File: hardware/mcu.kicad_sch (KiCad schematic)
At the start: 27 parts, among them J4 PROG, U6 RP2040, U9 IS25LP080D-JBLE, Y1 2TJ412000NYGBC

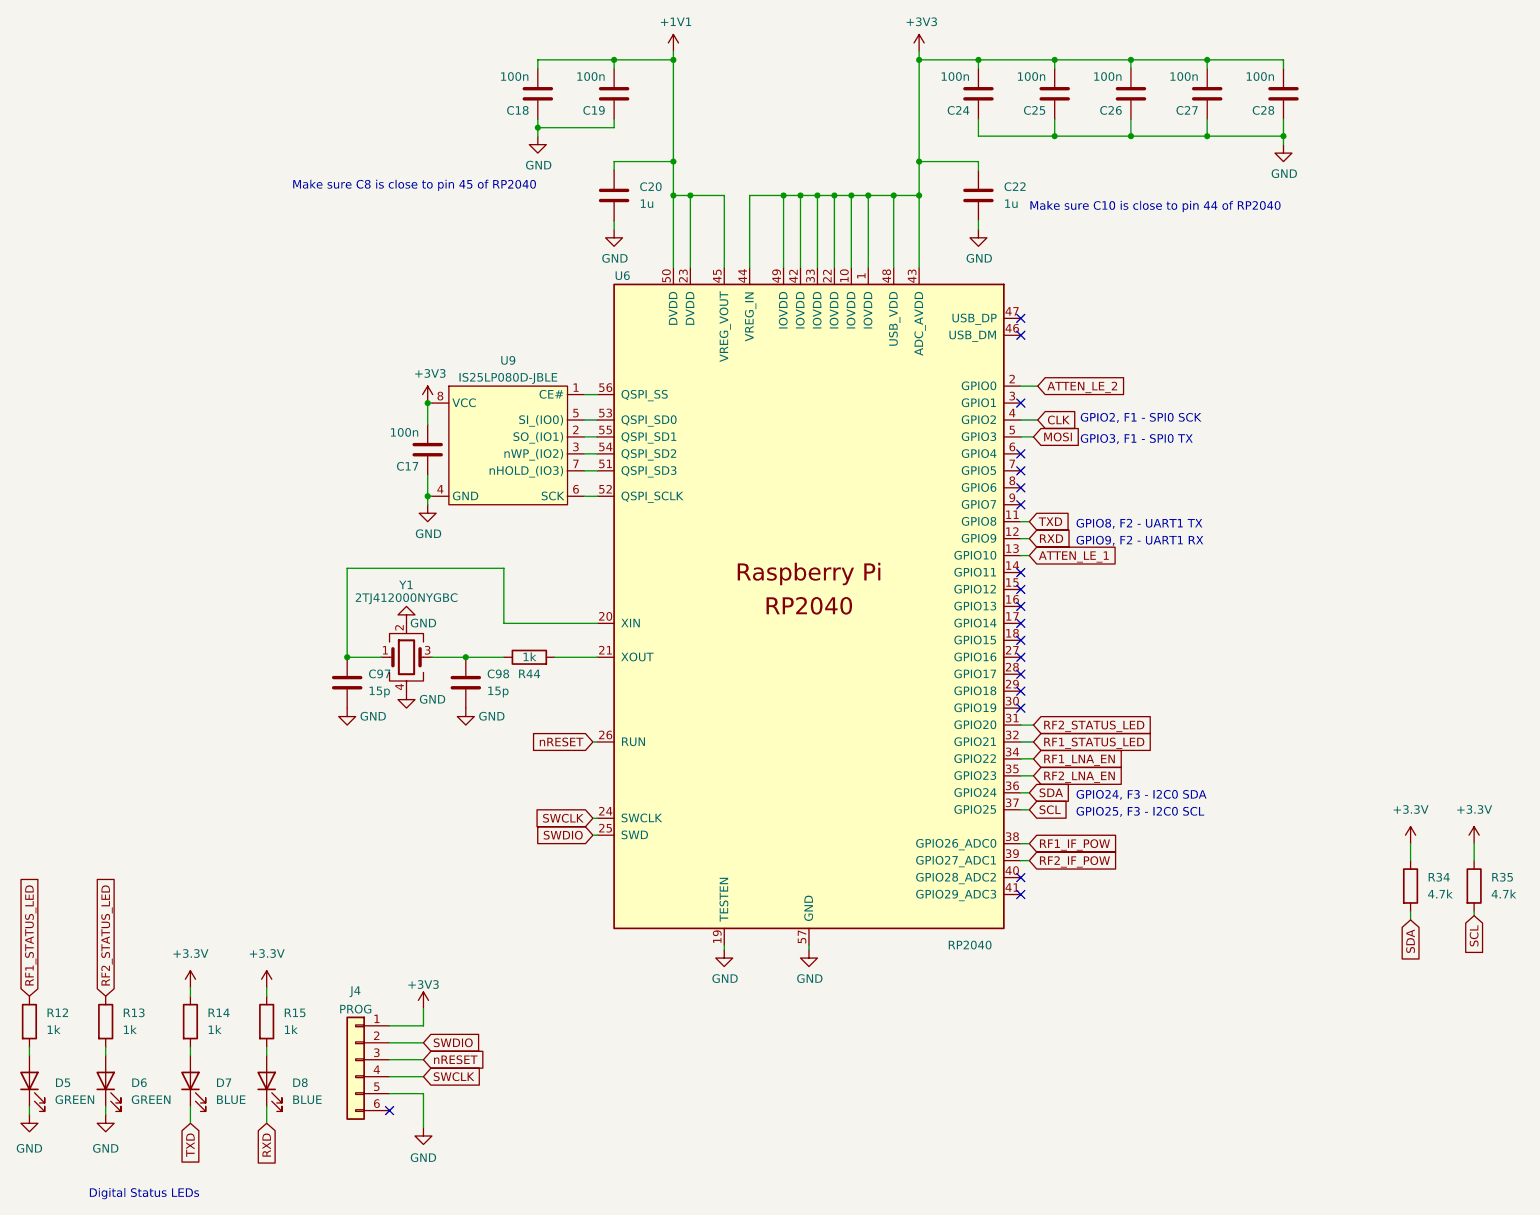
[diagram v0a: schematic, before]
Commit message: Update FEM hardware design for production version
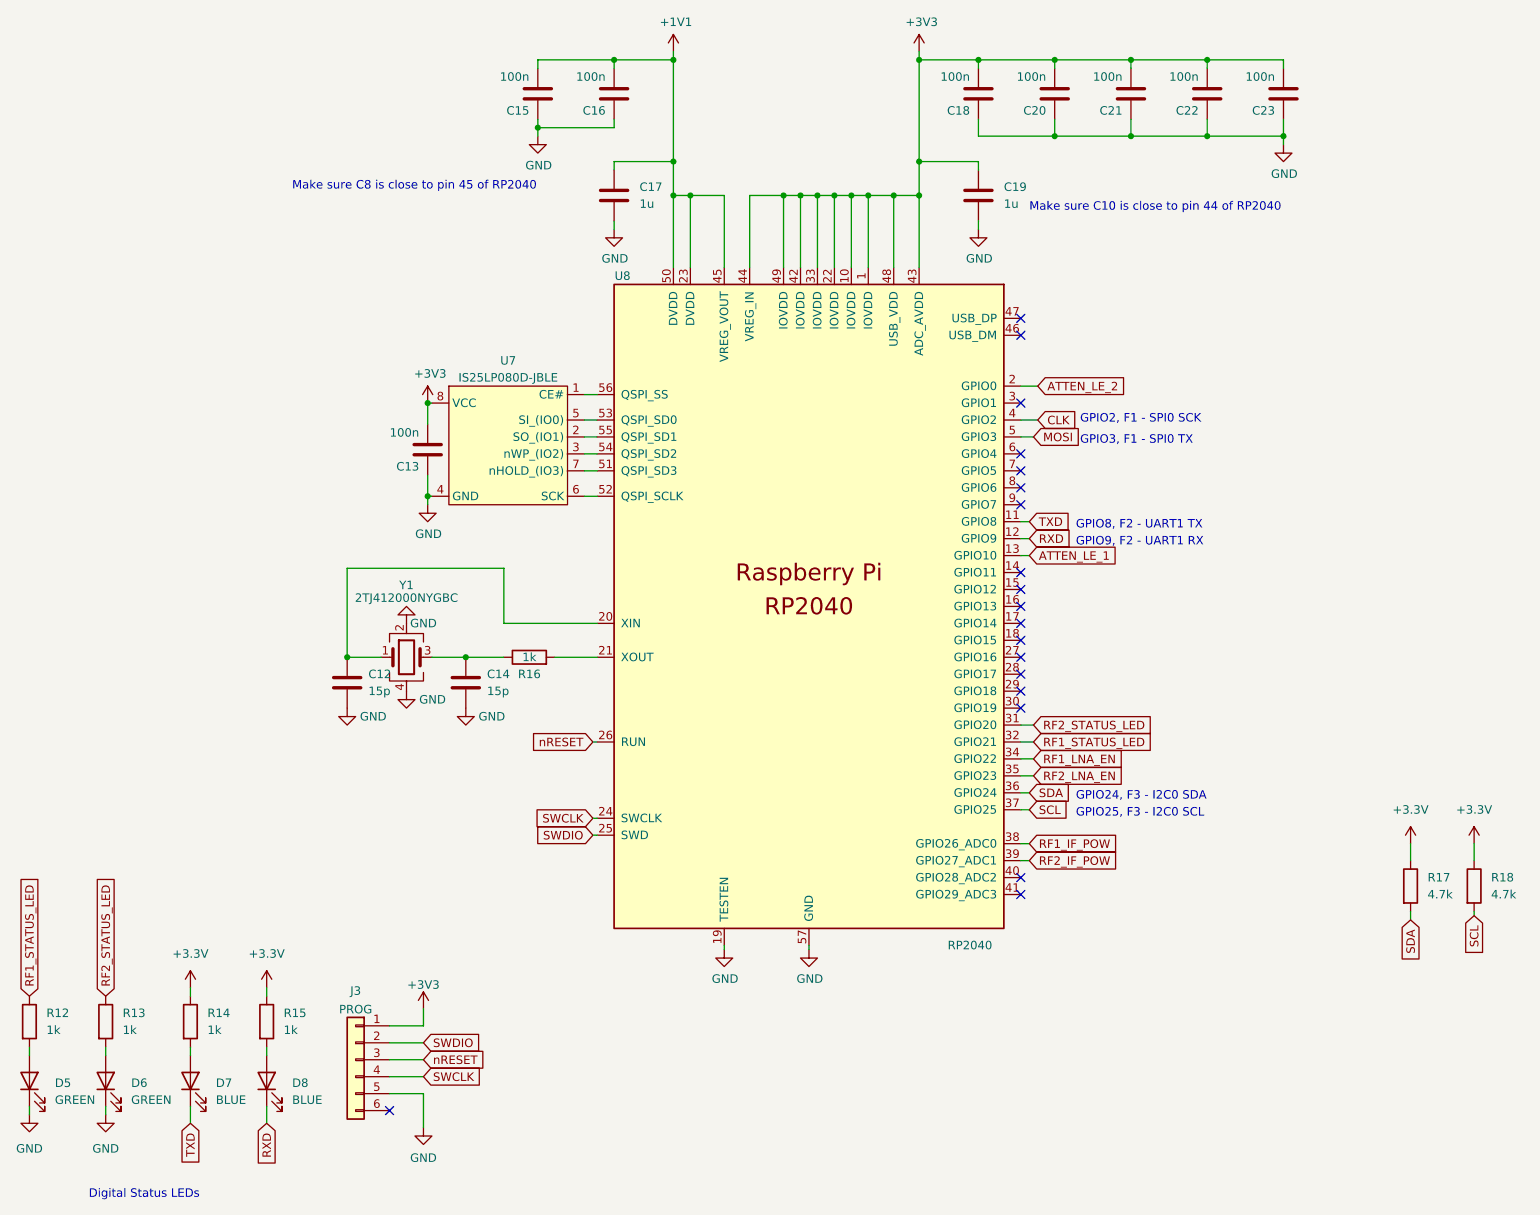
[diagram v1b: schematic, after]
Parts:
- renumbered C97 to C12, C17 to C13, C98 to C14, C18 to C15, C19 to C16, C20 to C17, C24 to C18, C22 to C19, C25 to C20, C26 to C21, C27 to C22, C28 to C23, J4 to J3, R44 to R16, R34 to R17, R35 to R18, U9 to U7, U6 to U8
